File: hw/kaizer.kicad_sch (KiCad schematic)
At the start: 26 parts, among them J1 from battery / PSU, J4 rpi zero 2w, Q1 BC337, Q2 BC337, Q3 IRF5305

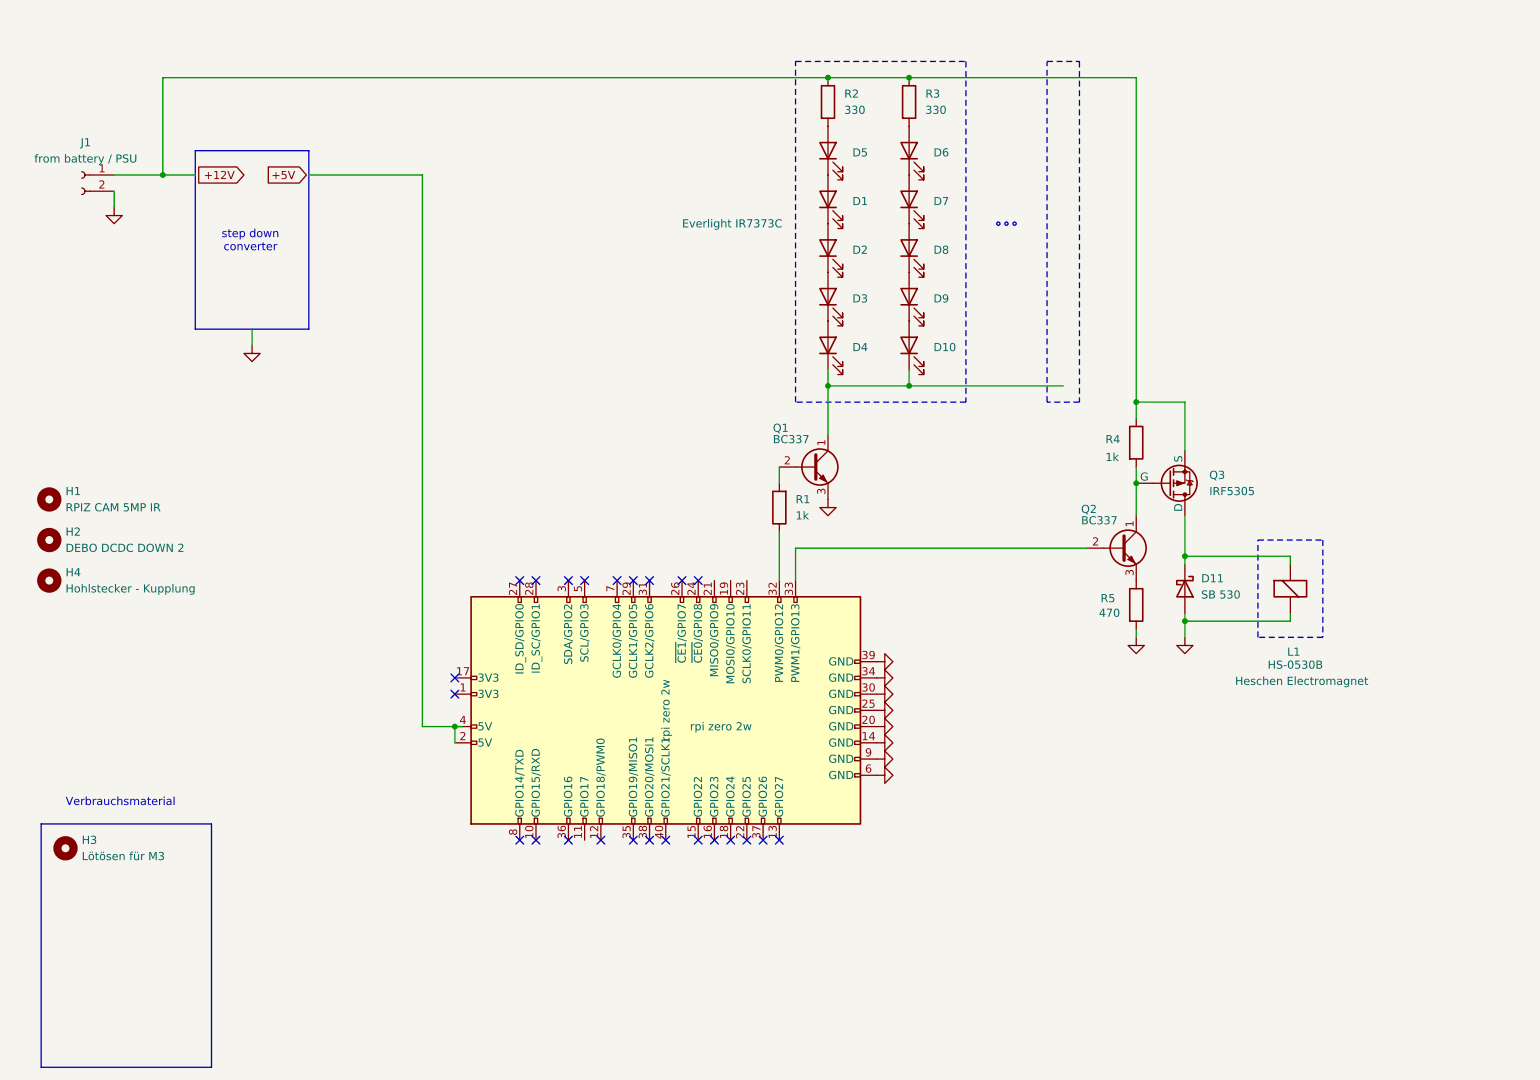
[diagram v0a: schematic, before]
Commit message: switch to battery powering
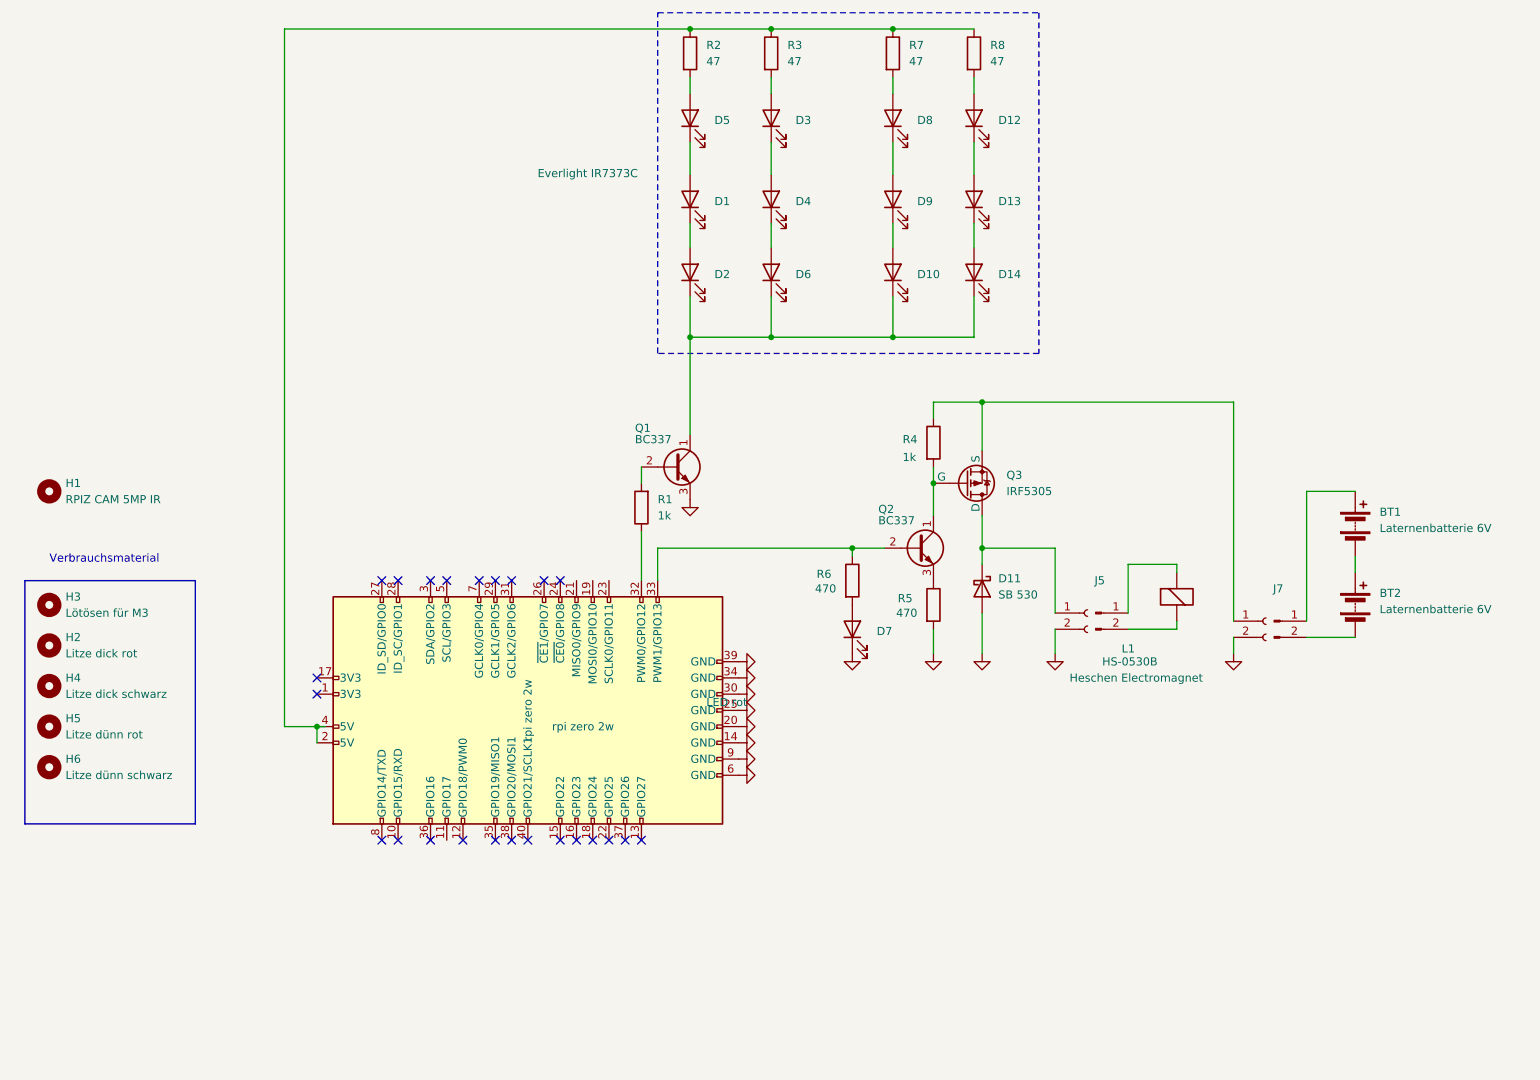
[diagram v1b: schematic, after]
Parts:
- removed J1: from battery / PSU, symbol Connector:Conn_01x02_Socket
- added BT1, BT2: Laternenbatterie 6V, symbol Device:Battery
- added D12, D13, D14: Everlight IR7373C, symbol Device:LED
- added H5: Litze dünn rot, symbol Mechanical:MountingHole
- added H6: Litze dünn schwarz, symbol Mechanical:MountingHole
- added J3, J6: Conn_01x02_Socket, symbol Connector:Conn_01x02_Socket
- added J5, J7: Schraubklemme, symbol Connector:Conn_01x02_Pin
- added R6: 470, symbol Device:R
- added R7, R8: 47, symbol Device:R
- D7: value Everlight IR7373C -> LED rot; ReicheltID IR 7373C EVL -> 3004R1C-DHE-A
- H2: value DEBO DCDC DOWN 2 -> Litze dick rot; ReicheltID DEBO DCDC DOWN 2 -> H05VK 1,0-10RT
- H4: value Hohlstecker - Kupplung -> Litze dick schwarz; ReicheltID HK 21 -> H05VK 1,0-10SW
- R2, R3: value 330 -> 47; ReicheltID 1/4W 330 -> 1/4W 47
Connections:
- net GNDA: now also D7.1 (K), J3.2 (Pin_2), J6.2 (Pin_2); no longer L1.2 (+)
- net at D6.1 (K): now also D10.1 (K), D2.1 (K), Q1.1 (C), D14.1 (K); no longer D7.2 (A)
- net at R3.2: now also D3.2 (A); no longer D6.2 (A)
- net at R2.1, R3.1: now also J4.2 (5V), J4.4 (5V), R7.1, R8.1; no longer Q3.3 (S), R4.1
- net at D11.1 (K), Q3.1 (D): now also J3.1 (Pin_1); no longer L1.1 (-)
- net at D8.2 (A): now also R7.2; no longer D7.1 (K)
- net at J4.33 (PWM1/GPIO13), Q2.2 (B): now also R6.1
- new net: D13.1 (K), D14.2 (A)
- new net: D12.1 (K), D13.2 (A)
- new net: D12.2 (A), R8.2
- new net: J6.1 (Pin_1), Q3.3 (S), R4.1
- new net: D4.1 (K), D6.2 (A)
- new net: BT1.1 (+), J7.1 (Pin_1)
- new net: BT2.2 (-), J7.2 (Pin_2)
- new net: J5.1 (Pin_1), L1.1 (-)
- new net: J5.2 (Pin_2), L1.2 (+)
- new net: D7.2 (A), R6.2
- new net: BT1.2 (-), BT2.1 (+)
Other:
- note removed: "step down converter"
- moved on the sheet: D1, D11, D2, D5, H1, H3, L1, Q1, Q2, Q3, R1, R2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
